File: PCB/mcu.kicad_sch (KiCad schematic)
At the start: 37 parts, among them J10 Conn_01x02, SW3 Reset, SW4 Boot, U1 LSM6DS3, U7 ESP32-S3, Y2 40MHz

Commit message: Production files
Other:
- note added: "Operating in "Mode 1""
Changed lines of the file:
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@@
+		)
+	)
+	(text "Operating in \"Mode 1\""
+		(exclude_from_sim no)
+		(at 30.226 145.034 0)
+		(effects
+			(font
+				(size 1.27 1.27)
+			)
 		)
 	)

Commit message: Updates to README
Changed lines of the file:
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@@
 	(text "MCU and peripherals"
 		(exclude_from_sim no)
-		(at 204.216 174.498 0)
+		(at 204.47 175.006 0)
 		(effects
 			(font
@@
 	(label "IO40"
 		(at 132.715 91.44 180)
-		(fields_autoplaced yes)
 		(effects
 			(font
@@
 	(label "IN[1..4]"
 		(at 137.16 154.94 0)
-		(fields_autoplaced yes)
 		(effects
 			(font
@@
 	(label "SDO"
 		(at 213.36 99.06 0)
-		(fields_autoplaced yes)
 		(effects
 			(font
@@
 	(label "IN1"
 		(at 125.73 147.32 180)
-		(fields_autoplaced yes)
 		(effects
 			(font
@@
 	(label "RX"
 		(at 217.17 60.96 0)
-		(fields_autoplaced yes)
 		(effects
 			(font
@@
 	(label "SDO"
 		(at 30.48 154.94 180)
-		(fields_autoplaced yes)
 		(effects
 			(font
@@
 	(label "SDA"
 		(at 213.36 101.6 0)
-		(fields_autoplaced yes)
 		(effects
 			(font
@@
 	(label "IN3"
 		(at 125.73 129.54 180)
-		(fields_autoplaced yes)
 		(effects
 			(font
@@
 	(label "CS"
 		(at 213.36 106.68 0)
-		(fields_autoplaced yes)
 		(effects
 			(font
@@
 	(label "IN2"
 		(at 125.73 119.38 180)
-		(fields_autoplaced yes)
 		(effects
 			(font
@@
 	(label "IN2"
 		(at 125.73 149.86 180)
-		(fields_autoplaced yes)
 		(effects
 			(font
@@
 	(label "SCL"
 		(at 213.36 104.14 0)
-		(fields_autoplaced yes)
 		(effects
 			(font
@@
 	(label "IO15"
 		(at 132.08 71.12 180)
-		(fields_autoplaced yes)
 		(effects
 			(font
@@
 	(label "IO41"
 		(at 132.715 93.98 180)
-		(fields_autoplaced yes)
 		(effects
 			(font
@@
 	(label "INT1"
 		(at 72.39 154.94 0)
-		(fields_autoplaced yes)
 		(effects
 			(font
@@
 	(label "IN4"
 		(at 125.73 152.4 180)
-		(fields_autoplaced yes)
 		(effects
 			(font
@@
 	(label "INT2"
 		(at 213.36 109.22 0)
-		(fields_autoplaced yes)
 		(effects
 			(font
@@
 	(label "INT1"
 		(at 212.725 96.52 0)
-		(fields_autoplaced yes)
 		(effects
 			(font
@@
 	(label "CS"
 		(at 25.4 170.18 180)
-		(fields_autoplaced yes)
 		(effects
 			(font
@@
 	(label "IO45"
 		(at 250.825 121.92 0)
-		(fields_autoplaced yes)
 		(effects
 			(font
@@
 	(label "IN1"
 		(at 125.73 121.92 180)
-		(fields_autoplaced yes)
 		(effects
 			(font
@@
 	(label "TX"
 		(at 217.17 58.42 0)
-		(fields_autoplaced yes)
 		(effects
 			(font
@@
 	(label "INT2"
 		(at 72.39 157.48 0)
-		(fields_autoplaced yes)
 		(effects
 			(font
@@
 	(label "IN4"
 		(at 125.73 127 180)
-		(fields_autoplaced yes)
 		(effects
 			(font
@@
 	(label "SDA"
 		(at 34.29 165.1 180)
-		(fields_autoplaced yes)
 		(effects
 			(font
@@
 	(label "IO42"
 		(at 132.715 96.52 180)
-		(fields_autoplaced yes)
 		(effects
 			(font
@@
 	(label "SCL"
 		(at 29.21 167.64 180)
-		(fields_autoplaced yes)
 		(effects
 			(font
@@
 	(label "IO16"
 		(at 132.08 73.66 180)
-		(fields_autoplaced yes)
 		(effects
 			(font
@@
 	(label "IN3"
 		(at 125.73 154.94 180)
-		(fields_autoplaced yes)
 		(effects
 			(font
@@
 		(shape output)
 		(at 154.94 154.94 0)
-		(fields_autoplaced yes)
 		(effects
 			(font
@@
 		(shape input)
 		(at 213.36 114.3 0)
-		(fields_autoplaced yes)
 		(effects
 			(font
@@
 		(shape bidirectional)
 		(at 214.63 66.04 0)
-		(fields_autoplaced yes)
 		(effects
 			(font
@@
 		(shape bidirectional)
 		(at 214.63 68.58 0)
-		(fields_autoplaced yes)
 		(effects
 			(font
@@
 		(shape input)
 		(at 219.71 93.98 0)
-		(fields_autoplaced yes)
 		(effects
 			(font
@@
 		(shape output)
 		(at 121.92 124.46 180)
-		(fields_autoplaced yes)
 		(effects
 			(font
@@
 		(shape input)
 		(at 218.44 119.38 0)
-		(fields_autoplaced yes)
-		(effects
-			(font
+		(effects
+			(font

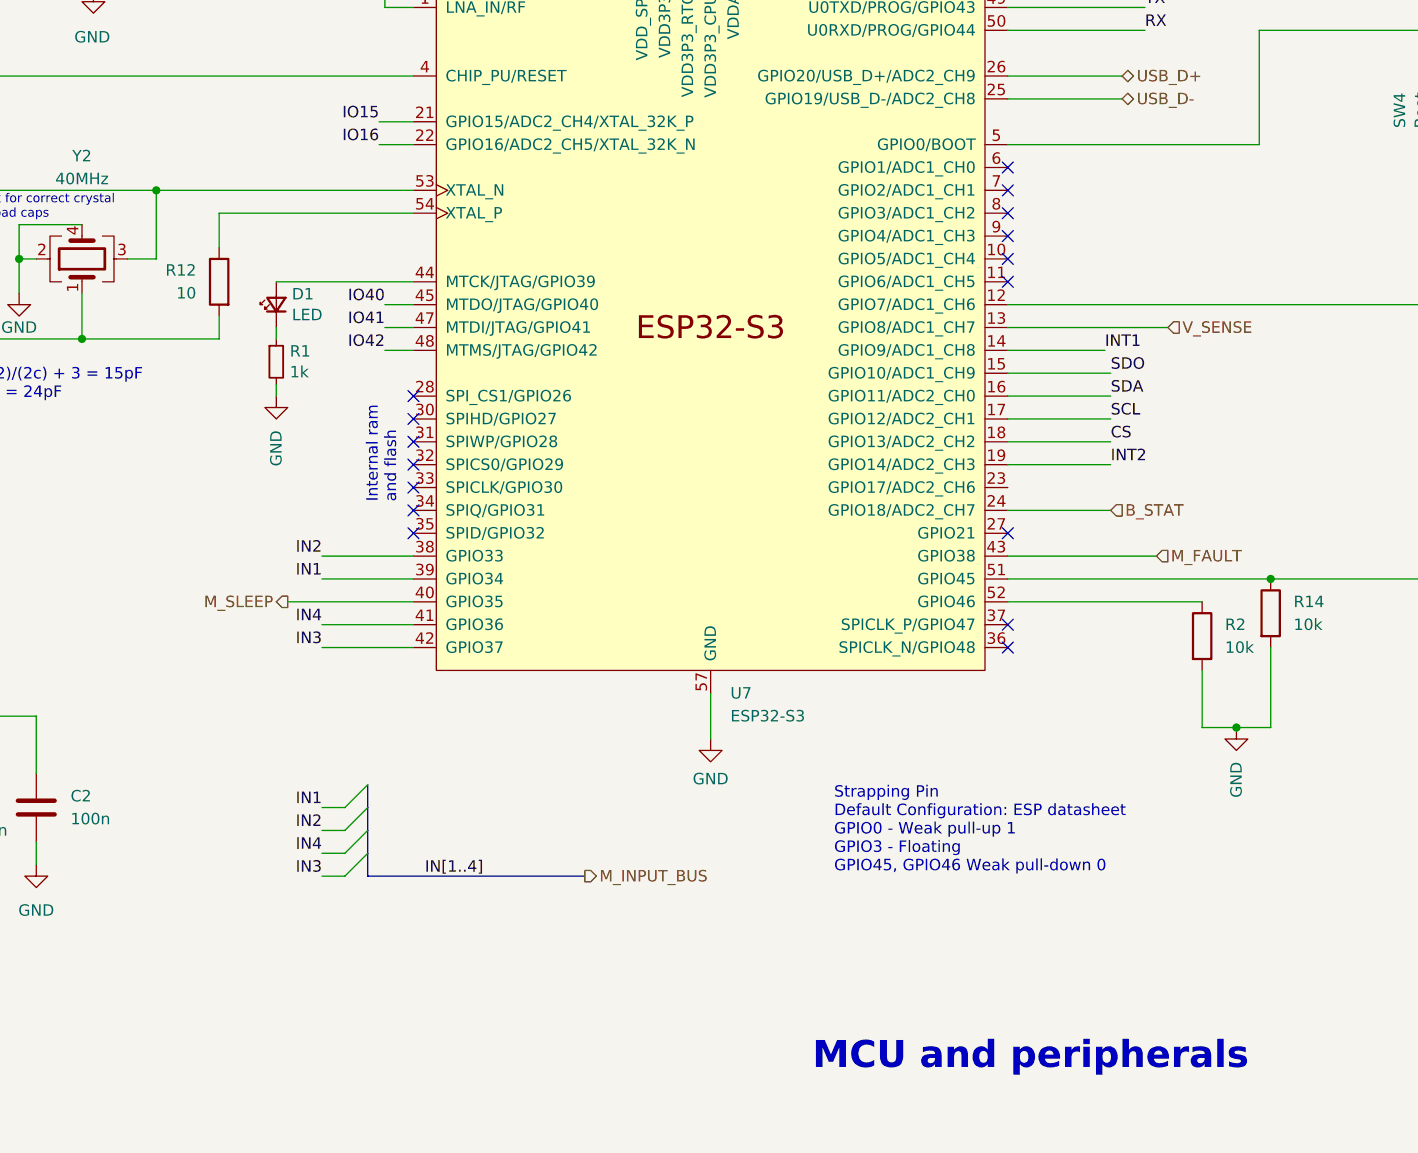
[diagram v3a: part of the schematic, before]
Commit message: Started design of Inverter
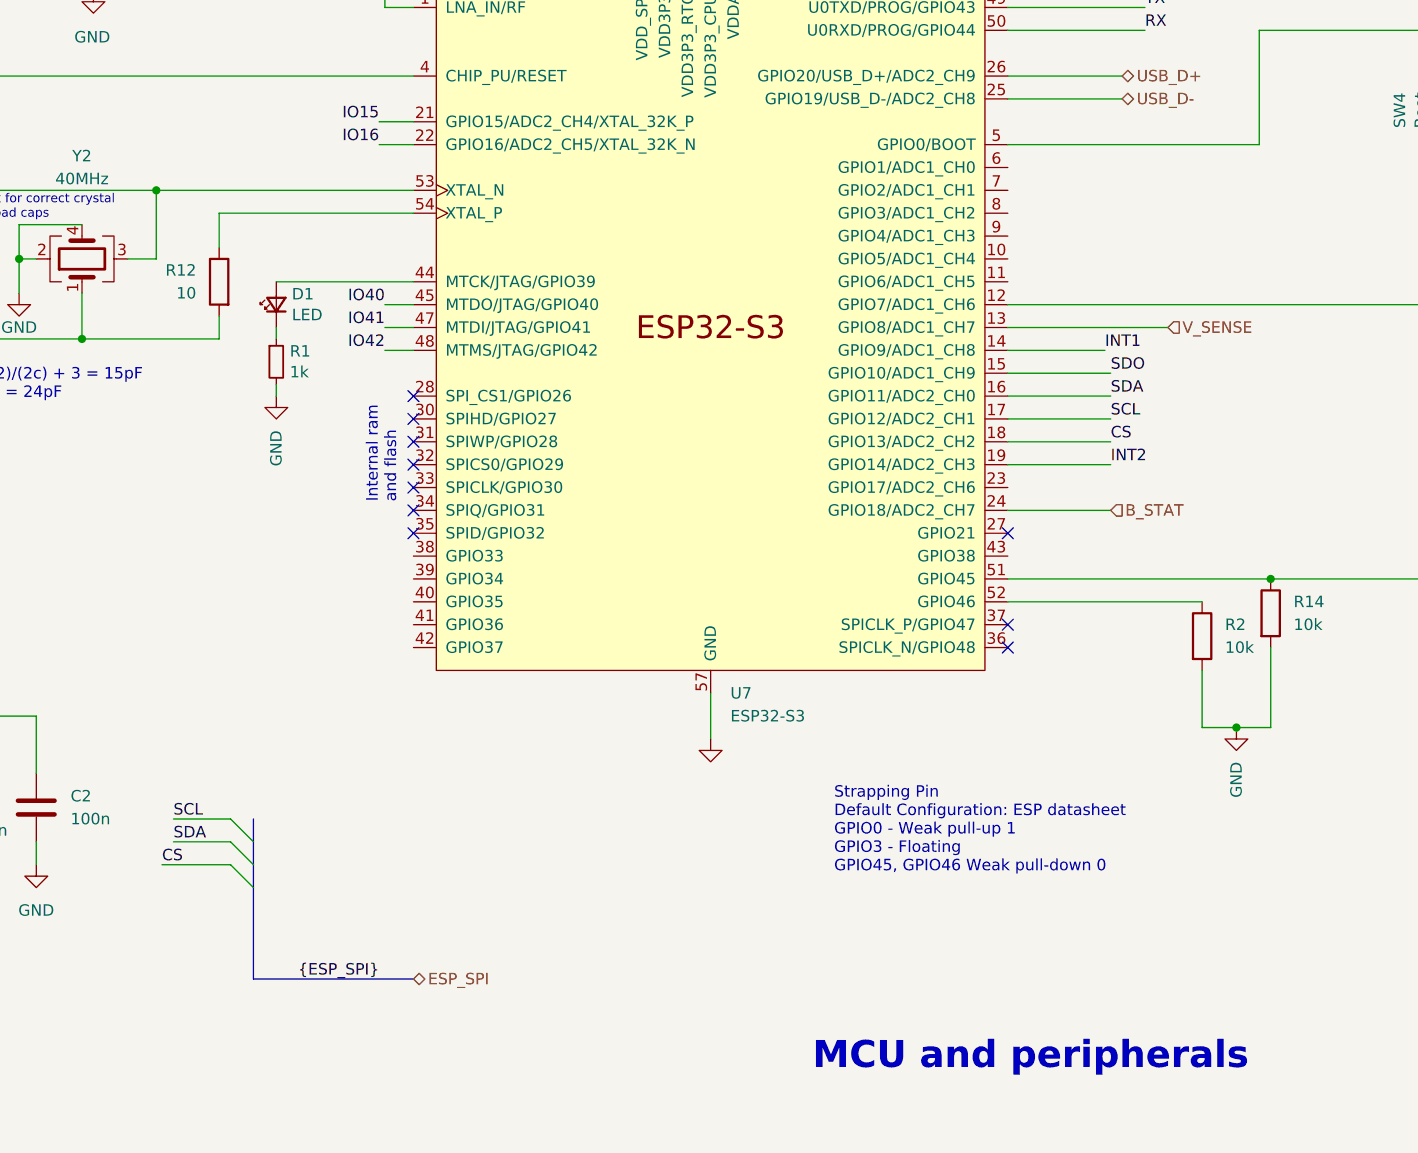
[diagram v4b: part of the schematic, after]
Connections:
- net IN1: no longer names the net of U7.39 (GPIO34)
- net IN2: no longer names the net of U7.38 (GPIO33)
- net IN3: no longer names the net of U7.42 (GPIO37)
- net IN4: no longer names the net of U7.41 (GPIO36)
- net M_FAULT: no longer names the net of U7.43 (GPIO38)
- net M_SLEEP: no longer names the net of U7.40 (GPIO35)
- no-connect marks 16 -> 10

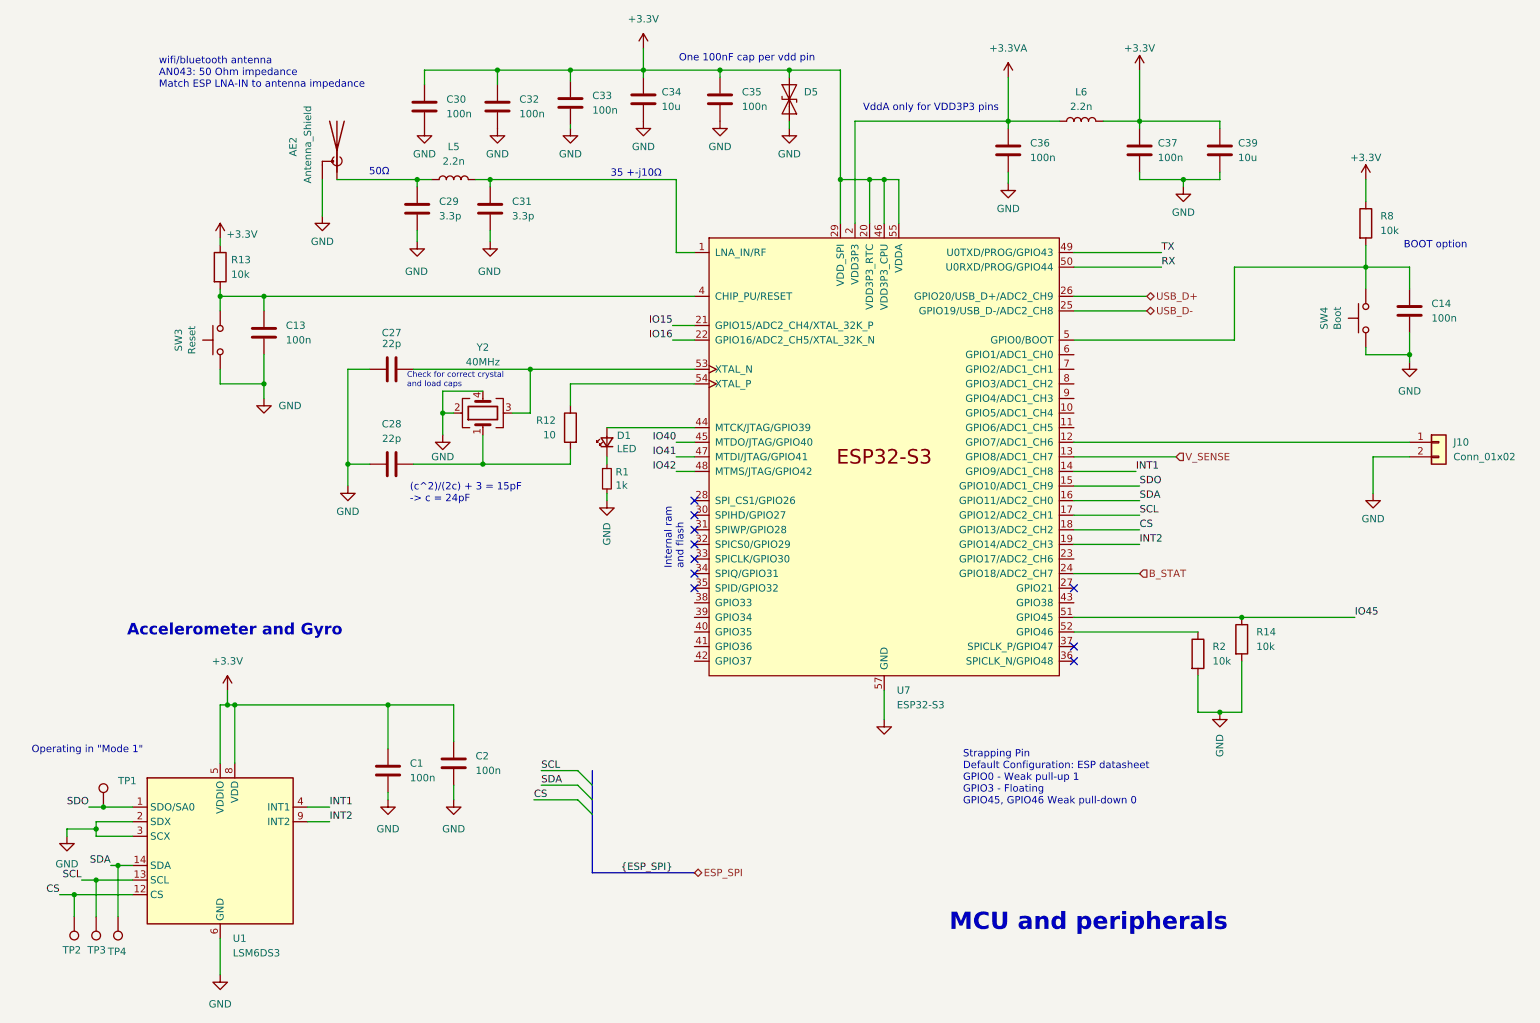
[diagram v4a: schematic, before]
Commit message: Hardware updates: STM32H7 and Inverted design
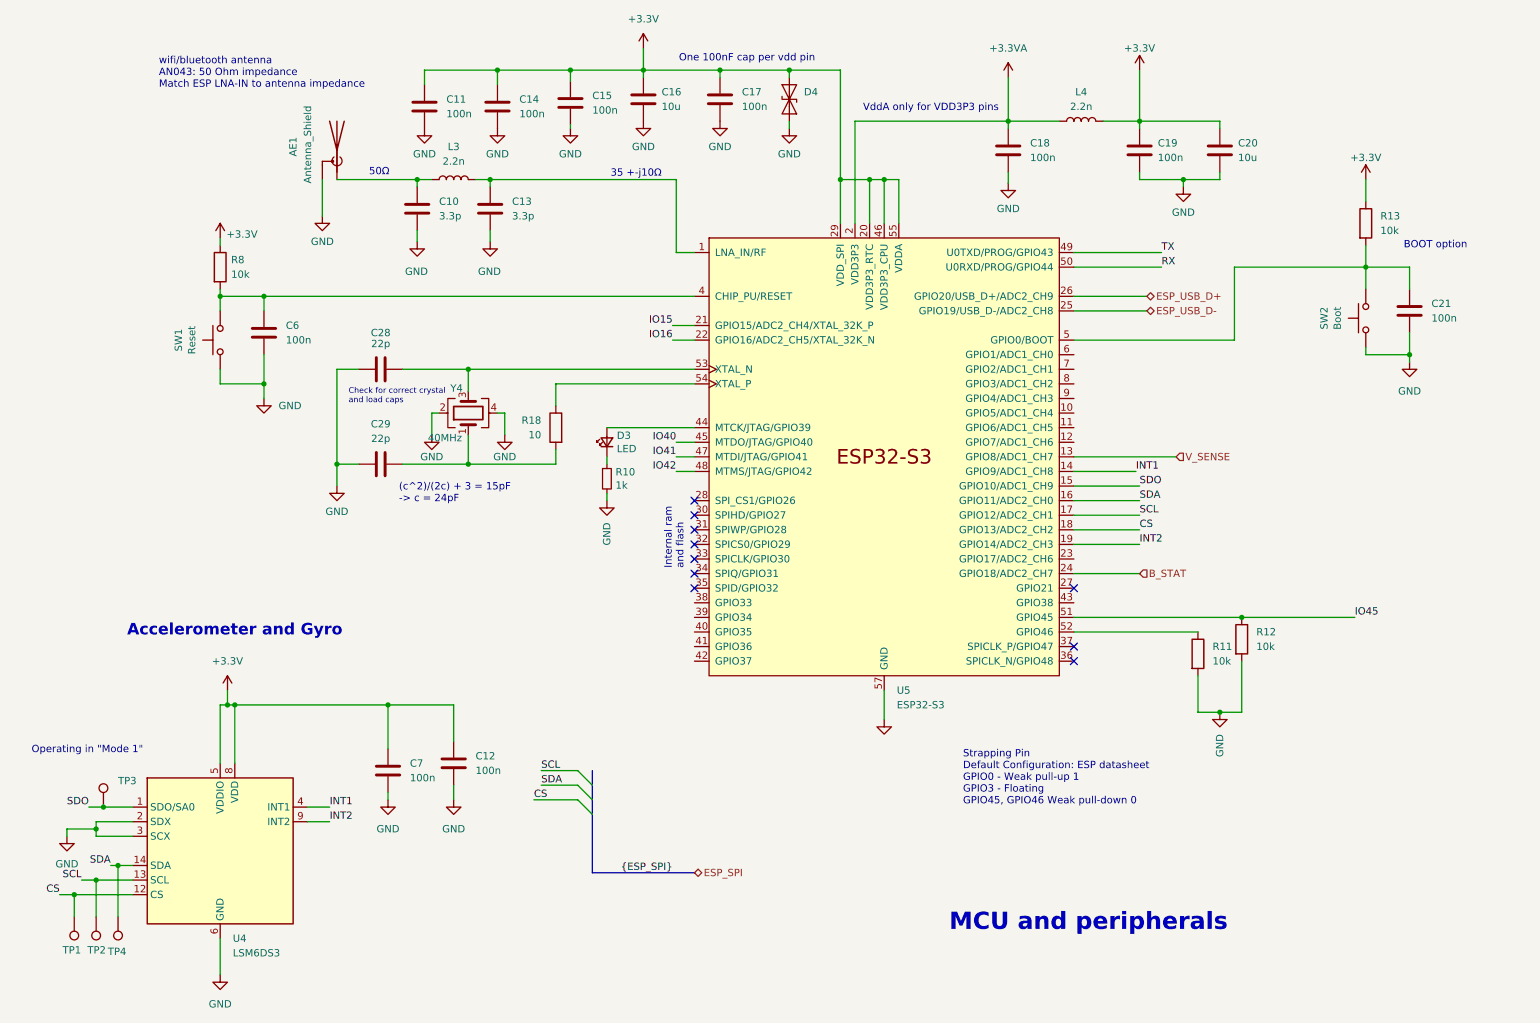
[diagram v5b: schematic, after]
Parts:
- removed C27: 22p, Capacitor_SMD:C_0402_1005Metric, symbol Device:C
- removed J10: Conn_01x02, Connector_PinHeader_2.54mm:PinHeader_1x02_P2.54mm_Vertical, symbol Connector_Generic:Conn_01x02
- removed R12: 10, Resistor_SMD:R_0402_1005Metric, symbol Device:R
- removed Y2: 40MHz, Crystal:Crystal_SMD_3225-4Pin_3.2x2.5mm, symbol Device:Crystal_GND23
- added C29: 22p, Capacitor_SMD:C_0402_1005Metric, symbol Device:C
- added R18: 10, Resistor_SMD:R_0402_1005Metric, symbol Device:R
- added Y4: 40MHz, Crystal:Crystal_SMD_3225-4Pin_3.2x2.5mm, symbol Device:Crystal_GND24
- renumbered AE2 to AE1, C29 to C10, C30 to C11, C2 to C12, C31 to C13, C32 to C14, C33 to C15, C34 to C16, C35 to C17, C36 to C18, C37 to C19, C39 to C20, C14 to C21, C13 to C6, C1 to C7, D1 to D3, D5 to D4, L5 to L3, L6 to L4, R1 to R10, R2 to R11, R14 to R12, R8 to R13, R13 to R8, SW3 to SW1, SW4 to SW2, TP2 to TP1, TP3 to TP2, TP1 to TP3, U1 to U4, U7 to U5
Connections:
- net GND: now also C29.1, Y4.2, Y4.4
- net at U5.53 (XTAL_N): now also C28.2, Y4.3
- net at U5.54 (XTAL_P): now also R18.1
- net USB_D+ renamed ESP_USB_D+
- net USB_D- renamed ESP_USB_D-
- new net: C29.2, R18.2, Y4.1

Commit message: Latest PCB version
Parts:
- AE1: footprint RF_Antenna:Texas_SWRA117D_2.4GHz_Left -> RF_Antenna:Texas_SWRA117D_2.4GHz_Right
- C10, C13: value 3.3p -> 2.2p
- L3: value 2.2n -> 2.6n
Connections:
- net CS: now also U5.41 (GPIO36)
- net MOSI: now reaches U5.38 (GPIO33)
- net MISO: now reaches U5.39 (GPIO34)
- net SCLK: now reaches U5.40 (GPIO35)
